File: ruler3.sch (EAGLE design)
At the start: 2 parts

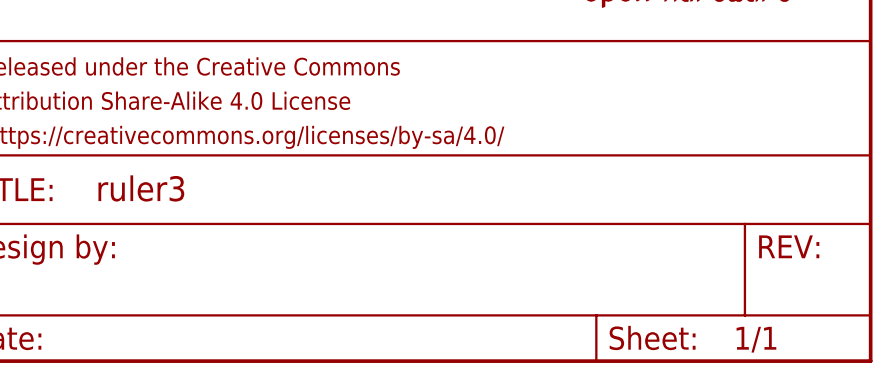
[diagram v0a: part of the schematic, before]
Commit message: Checklist
Update dimensions and a few text sizes to comply with the checklist
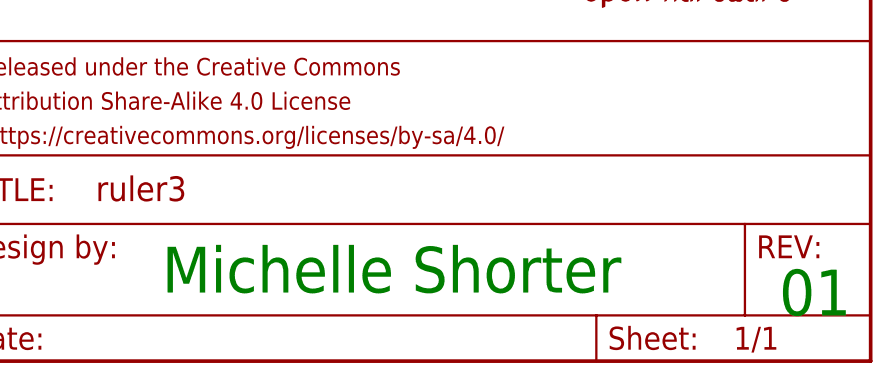
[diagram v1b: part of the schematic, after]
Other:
- note added: "01"
- note added: "Michelle Shorter"
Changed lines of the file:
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@@
 <sheet>
 <plain>
+<text x="170.18" y="7.62" size="5.08" layer="91">Michelle Shorter</text>
+<text x="238.76" y="5.08" size="5.08" layer="91">01</text>
 </plain>
 <instances>
